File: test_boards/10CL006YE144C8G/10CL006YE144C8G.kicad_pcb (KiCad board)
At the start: 2 copper layers, 92 parts, among them IC1 10CL006YE144C8G, J1 CL_JTAG, U1 W25Q128JVS, Y1 SG-7050CAN

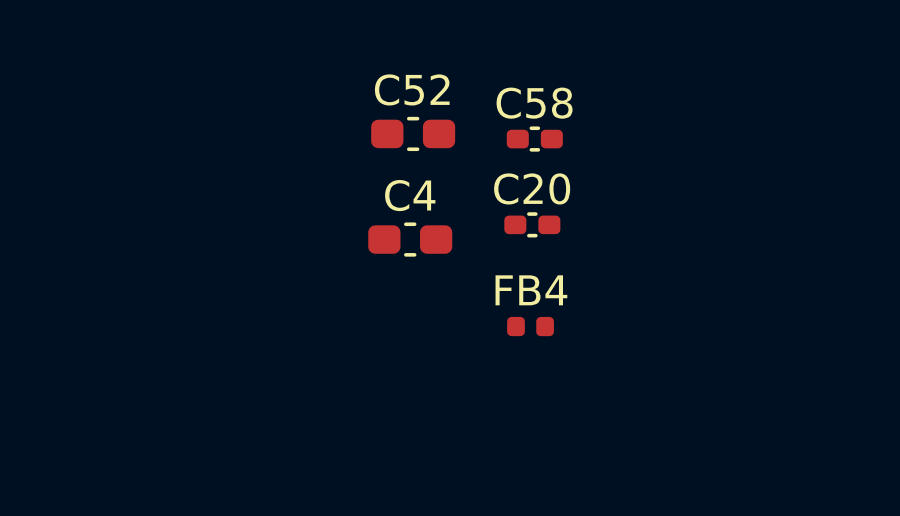
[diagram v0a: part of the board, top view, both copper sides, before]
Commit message: Клонирование дорожек работает!
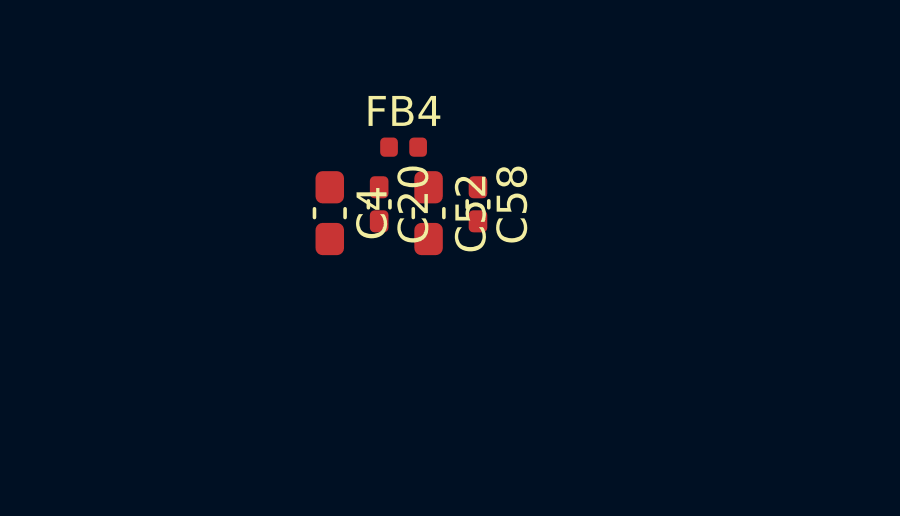
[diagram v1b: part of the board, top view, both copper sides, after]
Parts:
- moved FB4 7.33 mm to (112.8, 53.7)
- moved C20 5.15 mm to (112.0, 55.6), turned to -90 degrees
- moved C58 2.88 mm to (115.3, 55.6), turned to -90 degrees
- moved C4 2.82 mm to (110.3, 55.9), turned to -90 degrees
- moved C52 2.69 mm to (113.6, 55.9), turned to -90 degrees
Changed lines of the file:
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@@
 	(footprint "Capacitor_SMD:C_0402_1005Metric_Pad0.74x0.62mm_HandSolder"
 		(layer "F.Cu")
-		(at 117.185 53.47)
+		(at 115.29 55.645 -90)
 		(descr "Capacitor SMD 0402 (1005 Metric), square (rectangular) end terminal, IPC-7351 nominal with elongated pad for handsoldering. (Body size source: IPC-SM-782 page 76, https://www.pcb-3d.com/wordpress/wp-content/uploads/ipc-sm-782a_amendment_1_and_2.pdf)")
 		(tags "capacitor handsolder")
 		(property "Reference" "C58"
-			(at 0 -1.16 180)
+			(at 0 -1.16 90)
 			(layer "F.SilkS")
 			(effects
@@
 		)
 		(property "Value" "100 nF"
-			(at 0 1.16 180)
+			(at 0 1.16 90)
 			(layer "F.Fab")
 			(effects
@@
 		)
 		(property "Datasheet" ""
-			(at 0 0 180)
+			(at 0 0 90)
 			(layer "F.Fab")
 			(hide yes)
@@
 		)
 		(property "Description" "Unpolarized capacitor"
-			(at 0 0 180)
+			(at 0 0 90)
 			(layer "F.Fab")
 			(hide yes)
@@
 		)
 		(property "TemplateRole" "LIGHT"
-			(at 0 0 0)
+			(at 0 0 270)
 			(unlocked yes)
 			(layer "F.Fab")
@@
 		)
 		(property "Role" "PI_FILTER_C4"
-			(at 0 0 0)
+			(at 0 0 270)
 			(unlocked yes)
 			(layer "F.Fab")
@@
 		(duplicate_pad_numbers_are_jumpers no)
 		(fp_line
-			(start -0.115829 -0.36)
-			(end 0.115829 -0.36)
+			(start -0.115829 0.36)
+			(end 0.115829 0.36)
 			(stroke
 				(width 0.12)
@@
 		)
 		(fp_line
-			(start -0.115829 0.36)
-			(end 0.115829 0.36)
+			(start -0.115829 -0.36)
+			(end 0.115829 -0.36)
 			(stroke
 				(width 0.12)
@@
 		)
 		(fp_text user "${REFERENCE}"
-			(at 0 0 180)
+			(at 0 0 90)
 			(layer "F.Fab")
 			(effects
@@
 		)
 		(pad "1" smd roundrect
-			(at -0.5675 0)
+			(at -0.5675 0 270)
 			(size 0.735 0.62)
 			(layers "F.Cu" "F.Mask" "F.Paste")
@@
 		)
 		(pad "2" smd roundrect
-			(at 0.5675 0)
+			(at 0.5675 0 270)
 			(size 0.735 0.62)
 			(layers "F.Cu" "F.Mask" "F.Paste")
@@
 	(footprint "Capacitor_SMD:C_0603_1608Metric_Pad1.08x0.95mm_HandSolder"
 		(layer "F.Cu")
-		(at 113.0325 56.82)
+		(at 110.35 55.94 -90)
 		(descr "Capacitor SMD 0603 (1608 Metric), square (rectangular) end terminal, IPC-7351 nominal with elongated pad for handsoldering. (Body size source: IPC-SM-782 page 76, https://www.pcb-3d.com/wordpress/wp-content/uploads/ipc-sm-782a_amendment_1_and_2.pdf)")
 		(tags "capacitor handsolder")
 		(property "Reference" "C4"
-			(at 0 -1.43 0)
+			(at 0 -1.43 90)
 			(layer "F.SilkS")
 			(effects
@@
 		)
 		(property "Value" "1uF"
-			(at 0 1.43 0)
+			(at 0 1.43 90)
 			(layer "F.Fab")
 			(effects
@@
 		)
 		(property "Datasheet" ""
-			(at 0 0 0)
+			(at 0 0 90)
 			(layer "F.Fab")
 			(hide yes)
@@
 		)
 		(property "Description" "Unpolarized capacitor"
-			(at 0 0 0)
+			(at 0 0 90)
 			(layer "F.Fab")
 			(hide yes)
@@
 		)
 		(property "Role" "PI_FILTER_C1"
-			(at 0 0 0)
+			(at 0 0 270)
 			(unlocked yes)
 			(layer "F.Fab")
@@
 		(duplicate_pad_numbers_are_jumpers no)
 		(fp_line
-			(start -0.146267 -0.51)
-			(end 0.146267 -0.51)
+			(start -0.146267 0.51)
+			(end 0.146267 0.51)
 			(stroke
 				(width 0.12)
@@
 		)
 		(fp_line
-			(start -0.146267 0.51)
-			(end 0.146267 0.51)
+			(start -0.146267 -0.51)
+			(end 0.146267 -0.51)
 			(stroke
 				(width 0.12)
@@
 		)
 		(fp_text user "${REFERENCE}"
-			(at 0 0 0)
+			(at 0 0 90)
 			(layer "F.Fab")
 			(effects
@@
 		)
 		(pad "1" smd roundrect
-			(at -0.8625 0)
+			(at -0.8625 0 270)
 			(size 1.075 0.95)
 			(layers "F.Cu" "F.Mask" "F.Paste")
@@
 		)
 		(pad "2" smd roundrect
-			(at 0.8625 0)
+			(at 0.8625 0 270)
 			(size 1.075 0.95)
 			(layers "F.Cu" "F.Mask" "F.Paste")
@@
 	(footprint "Inductor_SMD:L_0402_1005Metric"
 		(layer "F.Cu")
-		(at 117.0425 59.72)
+		(at 112.81 53.74)
 		(descr "Inductor SMD 0402 (1005 Metric), square (rectangular) end terminal, IPC-7351 nominal, (Body size source: http://www.tortai-tech.com/upload/download/2011102023233369053.pdf)")
 		(tags "inductor")
@@
 		)
 		(property "Value" "BLM15PD121SN1D"
-			(at 0 1.17 0)
+			(at 0 -1.25 0)
 			(layer "F.Fab")
 			(effects
@@
 	(footprint "Capacitor_SMD:C_0603_1608Metric_Pad1.08x0.95mm_HandSolder"
 		(layer "F.Cu")
-		(at 113.13 53.3)
+		(at 113.643333 55.94 -90)
 		(descr "Capacitor SMD 0603 (1608 Metric), square (rectangular) end terminal, IPC-7351 nominal with elongated pad for handsoldering. (Body size source: IPC-SM-782 page 76, https://www.pcb-3d.com/wordpress/wp-content/uploads/ipc-sm-782a_amendment_1_and_2.pdf)")
 		(tags "capacitor handsolder")
 		(property "Reference" "C52"
-			(at 0 -1.43 180)
+			(at 0 -1.43 90)
 			(layer "F.SilkS")
 			(effects
@@
 		)
 		(property "Value" "1uF"
-			(at 0 1.43 180)
+			(at 0 1.43 90)
 			(layer "F.Fab")
 			(effects
@@
 		)
 		(property "Datasheet" ""
-			(at 0 0 180)
+			(at 0 0 90)
 			(layer "F.Fab")
 			(hide yes)
@@
 		)
 		(property "Description" "Unpolarized capacitor"
-			(at 0 0 180)
+			(at 0 0 90)
 			(layer "F.Fab")
 			(hide yes)
@@
 		)
 		(property "Role" "PI_FILTER_C3"
-			(at 0 0 0)
+			(at 0 0 270)
 			(unlocked yes)
 			(layer "F.Fab")
@@
 		(duplicate_pad_numbers_are_jumpers no)
 		(fp_line
-			(start -0.146261 -0.51)
-			(end 0.146261 -0.51)
+			(start -0.146261 0.51)
+			(end 0.146261 0.51)
 			(stroke
 				(width 0.12)
@@
 		)
 		(fp_line
-			(start -0.146261 0.51)
-			(end 0.146261 0.51)
+			(start -0.146261 -0.51)
+			(end 0.146261 -0.51)
 			(stroke
 				(width 0.12)
@@
 		)
 		(fp_text user "${REFERENCE}"
-			(at 0 0 180)
+			(at 0 0 90)
 			(layer "F.Fab")
 			(effects
@@
 		)
 		(pad "1" smd roundrect
-			(at -0.8625 0)
+			(at -0.8625 0 270)
 			(size 1.075 0.95)
 			(layers "F.Cu" "F.Mask" "F.Paste")
@@
 		)
 		(pad "2" smd roundrect
-			(at 0.8625 0)
+			(at 0.8625 0 270)
 			(size 1.075 0.95)
 			(layers "F.Cu" "F.Mask" "F.Paste")
@@
 	(footprint "Capacitor_SMD:C_0402_1005Metric_Pad0.74x0.62mm_HandSolder"
 		(layer "F.Cu")
-		(at 117.1025 56.33)
+		(at 111.996667 55.645 -90)
 		(descr "Capacitor SMD 0402 (1005 Metric), square (rectangular) end terminal, IPC-7351 nominal with elongated pad for handsoldering. (Body size source: IPC-SM-782 page 76, https://www.pcb-3d.com/wordpress/wp-content/uploads/ipc-sm-782a_amendment_1_and_2.pdf)")
 		(tags "capacitor handsolder")
 		(property "Reference" "C20"
-			(at 0 -1.16 0)
+			(at 0 -1.16 90)
 			(layer "F.SilkS")
 			(effects
@@
 		)
 		(property "Value" "100 nF"
-			(at 0 1.16 0)
+			(at 0 1.16 90)
 			(layer "F.Fab")
 			(effects
@@
 		)
 		(property "Datasheet" ""
-			(at 0 0 0)
+			(at 0 0 90)
 			(layer "F.Fab")
 			(hide yes)
@@
 		)
 		(property "Description" "Unpolarized capacitor"
-			(at 0 0 0)
+			(at 0 0 90)
 			(layer "F.Fab")
 			(hide yes)
@@
 		)
 		(property "Role" "PI_FILTER_C2"
-			(at 0 0 0)
+			(at 0 0 270)
 			(unlocked yes)
 			(layer "F.Fab")
@@
 		(duplicate_pad_numbers_are_jumpers no)
 		(fp_line
-			(start -0.115835 -0.36)
-			(end 0.115835 -0.36)
+			(start -0.115835 0.36)
+			(end 0.115835 0.36)
 			(stroke
 				(width 0.12)
@@
 		)
 		(fp_line
-			(start -0.115835 0.36)
-			(end 0.115835 0.36)
+			(start -0.115835 -0.36)
+			(end 0.115835 -0.36)
 			(stroke
 				(width 0.12)
@@
 		)
 		(fp_text user "${REFERENCE}"
-			(at 0 0 0)
+			(at 0 0 90)
 			(layer "F.Fab")
 			(effects
@@
 		)
 		(pad "1" smd roundrect
-			(at -0.5675 0)
+			(at -0.5675 0 270)
 			(size 0.735 0.62)
 			(layers "F.Cu" "F.Mask" "F.Paste")
@@
 		)
 		(pad "2" smd roundrect
-			(at 0.5675 0)
+			(at 0.5675 0 270)
 			(size 0.735 0.62)
 			(layers "F.Cu" "F.Mask" "F.Paste")

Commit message: Добавлен проект для тестового клонирования.
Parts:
- C10, C11, C12, C13, C14, C15, C16, C20, C21, C22, C23, C24, C25, C26, C27, C28, C29, C30, C31, C32, C33, C34, C35, C36, C37, C38, C39, C4, C40, C41, C42, C43, C44, C45, C46, C47, C48, C5, C52, C53, C54, C58, C59, C6, C60, C61, C62, C63, C64, C7, C8, C9, FB4: moved to B.Cu
- moved C63 133.9 mm to (66.7, 84.6), turned to 180 degrees
- moved C61 130.6 mm to (69.7, 84.6)
- moved C41 128.3 mm to (66.7, 70.6), turned to 180 degrees
- moved C59 127.6 mm to (72.2, 89.1), turned to -90 degrees
- moved C42 126.4 mm to (66.7, 81.8), turned to 180 degrees
- moved C48 125.5 mm to (74.4, 63.6), turned to 90 degrees
- moved C32 124.2 mm to (72.2, 63.6), turned to 90 degrees
- moved C21 121.3 mm to (66.7, 76.6), turned to 180 degrees
- moved C22 121.3 mm to (66.7, 79.3), turned to 180 degrees
- moved C31 119.2 mm to (76.7, 63.6), turned to 90 degrees
- moved C33 119.1 mm to (69.7, 70.6)
- moved C43 118.8 mm to (76.7, 89.1), turned to -90 degrees
- moved C60 118.2 mm to (85.7, 63.6), turned to 90 degrees
- moved C40 117.8 mm to (74.4, 66.6), turned to -90 degrees
- moved C30 116.3 mm to (78.9, 63.6), turned to 90 degrees
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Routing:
- net GND: track 0.00 -> 10.5 mm, vias 0 -> 68
- net +3V3: track 0.00 -> 4.81 mm, vias 0 -> 1
- net +3V3_VCCIO: track 0.00 -> 4.44 mm, vias 0 -> 13
- net +2V5_VCCA: vias 0 -> 2
- net +1V2_VCCINT: vias 0 -> 8
- net +1V2_VCCD_PLL: vias 0 -> 2
